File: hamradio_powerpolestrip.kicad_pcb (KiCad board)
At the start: 2 copper layers, 145 x 50 mm, 27 parts, among them J1 Conn_01x02_Pin, J2 Conn_01x02_Pin, J3 Conn_01x02_Pin, J4 Conn_01x02_Pin, J5 Conn_01x02_Pin, J6 Conn_01x02_Pin, J7 Conn_01x02_Pin, J8 Conn_01x02_Pin

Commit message: updates
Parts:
- added G***: LOGO, Library:qrcode_15mm, F.Cu at (153.0, 109.0)
- moved D1 3.61 mm to (108.0, 82.5)
- moved R1 2.50 mm to (104.0, 82.5)
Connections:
- H1 pad 1: (no net) -> GND
- H2 pad 1: (no net) -> GND
- H3 pad 1: (no net) -> GND
- H4 pad 1: (no net) -> GND
- H5 pad 1: (no net) -> GND
- H6 pad 1: (no net) -> GND
- H7 pad 1: (no net) -> GND
- H8 pad 1: (no net) -> GND
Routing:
- net Net-(D1-K): track 0.00 -> 4.00 mm
- net +BATT: track 0.00 -> 2.71 mm, vias 0 -> 124
- net Net-(J8-Pin_1): vias 0 -> 14
- net Net-(J7-Pin_1): vias 0 -> 14
- net Net-(J6-Pin_1): vias 0 -> 14
- net Net-(J5-Pin_1): vias 0 -> 14
- net Net-(J4-Pin_1): vias 0 -> 14
- net Net-(J3-Pin_1): vias 0 -> 14
- net Net-(J2-Pin_1): vias 0 -> 14
- net Net-(J1-Pin_2): vias 0 -> 22
- net Net-(J1-Pin_1): vias 0 -> 23
- net GND: vias 0 -> 102
- added copper zone on B.Cu, net +BATT
- added copper zone on F.Cu, net GND
- added copper zone on B.Cu, net Net-(J1-Pin_1)
- added copper zone on B.Cu, net Net-(J1-Pin_2)
- added copper zone on B.Cu, net Net-(J2-Pin_1)
- added copper zone on B.Cu, net Net-(J3-Pin_1)
- added copper zone on B.Cu, net Net-(J4-Pin_1)
- added copper zone on B.Cu, net Net-(J5-Pin_1)
- added copper zone on B.Cu, net Net-(J6-Pin_1)
- added copper zone on B.Cu, net Net-(J7-Pin_1)
- added copper zone on B.Cu, net Net-(J8-Pin_1)
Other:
- board size 145 x 50 mm -> 147.2 x 50.7 mm
- board text added: "30A MAX! USE ATC/ATO FUSES"
- board text added: "DEREK - NZ0P gx1400@gmail.com 2024"
- board text added: "JLCJLCJLCJLC"
- board text added: "LICENSE GPLv3"
- board text added: "POWERPOLE POWER STRIP"

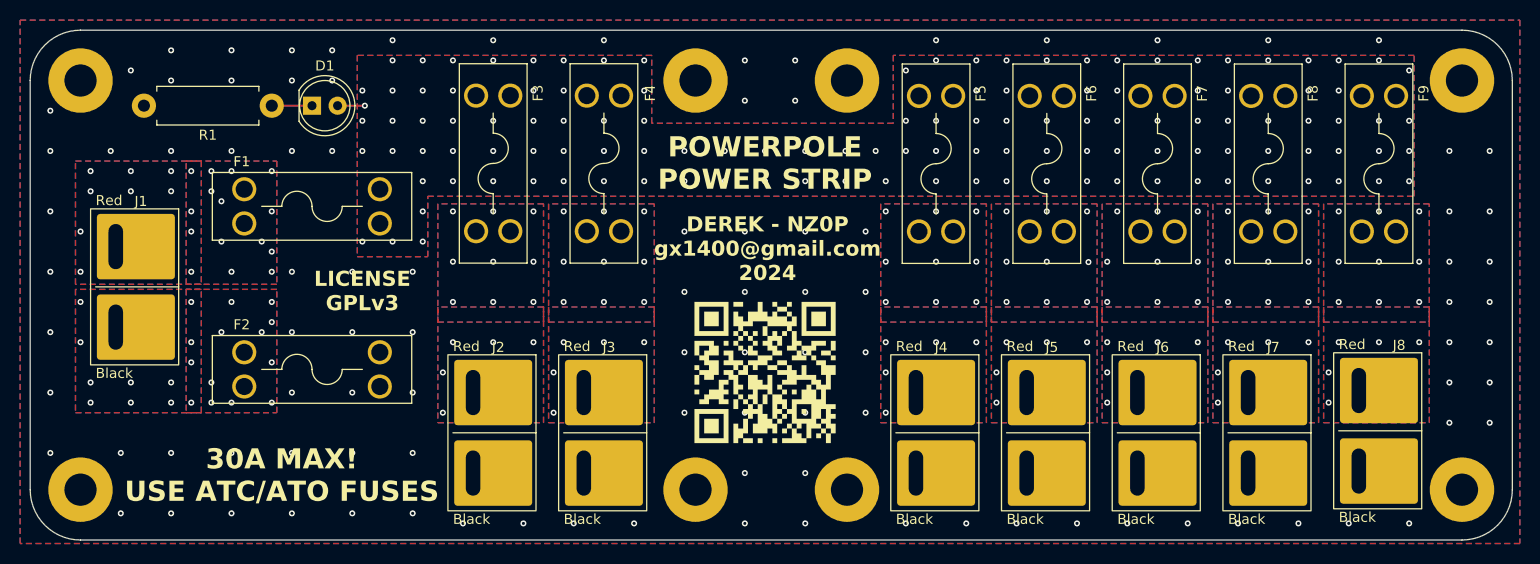
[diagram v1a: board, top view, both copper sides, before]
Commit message: reduce size of board 1mm each direction
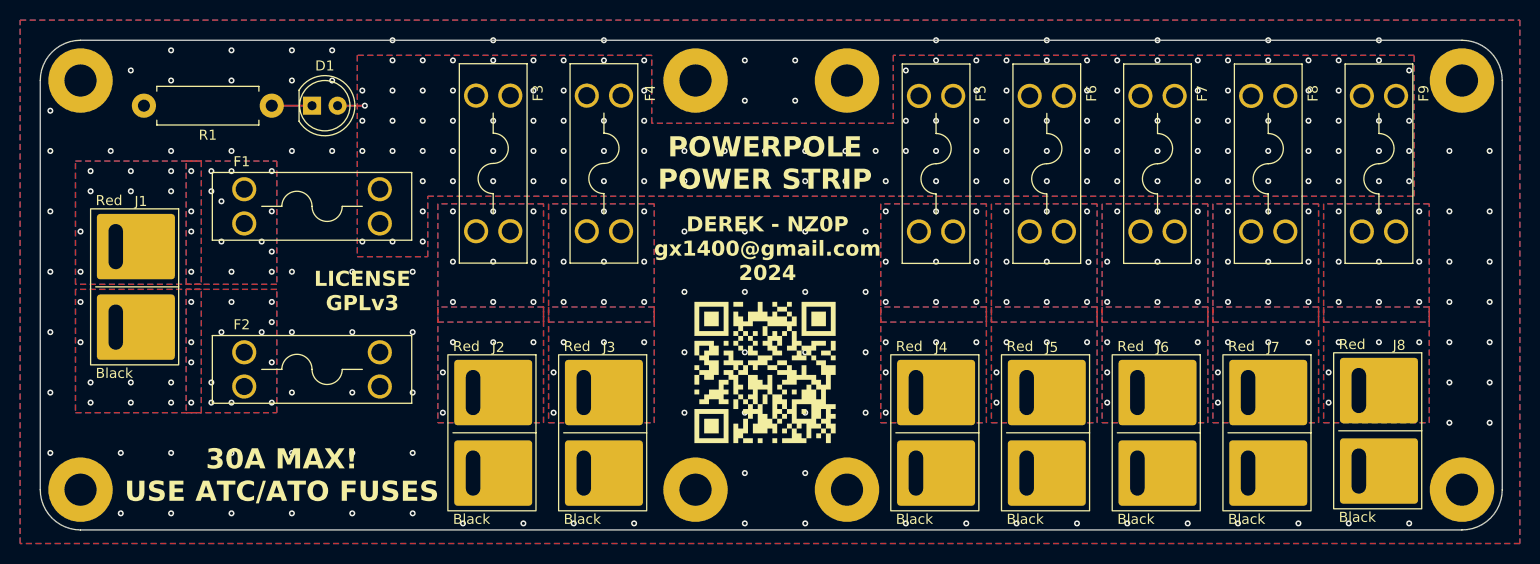
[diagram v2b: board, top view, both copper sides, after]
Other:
- board size 147.2 x 50.7 mm -> 145.2 x 48.7 mm
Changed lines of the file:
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@@
 	)
 	(gr_arc
-		(start 85 125.65)
-		(mid 81.464466 124.185534)
-		(end 80 120.65)
+		(start 85 124.65)
+		(mid 82.171573 123.478427)
+		(end 81 120.65)
 		(locked yes)
 		(stroke
@@
 	)
 	(gr_arc
-		(start 227.25 120.65)
-		(mid 225.785534 124.185534)
-		(end 222.25 125.65)
+		(start 226.25 120.65)
+		(mid 225.078427 123.478427)
+		(end 222.25 124.65)
 		(locked yes)
 		(stroke
@@
 	)
 	(gr_arc
-		(start 222.25 75)
-		(mid 225.785534 76.464466)
-		(end 227.25 80)
+		(start 222.25 76)
+		(mid 225.078427 77.171573)
+		(end 226.25 80)
 		(locked yes)
 		(stroke
@@
 	)
 	(gr_line
-		(start 222.25 75)
-		(end 85 75)
+		(start 222.25 76)
+		(end 85 76)
 		(locked yes)
 		(stroke
@@
 	)
 	(gr_line
-		(start 80 80)
-		(end 80 120.65)
+		(start 81 80)
+		(end 81 120.65)
 		(locked yes)
 		(stroke
@@
 	)
 	(gr_arc
-		(start 80 80)
-		(mid 81.464466 76.464466)
-		(end 85 75)
+		(start 81 80)
+		(mid 82.171573 77.171573)
+		(end 85 76)
 		(locked yes)
 		(stroke
@@
 	)
 	(gr_line
-		(start 227.25 80)
-		(end 227.25 120.65)
+		(start 226.25 80)
+		(end 226.25 120.65)
 		(locked yes)
 		(stroke
@@
 	)
 	(gr_line
-		(start 85 125.65)
-		(end 222.25 125.65)
+		(start 85 124.65)
+		(end 222.25 124.65)
 		(locked yes)
 		(stroke
